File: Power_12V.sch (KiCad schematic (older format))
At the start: 5 parts

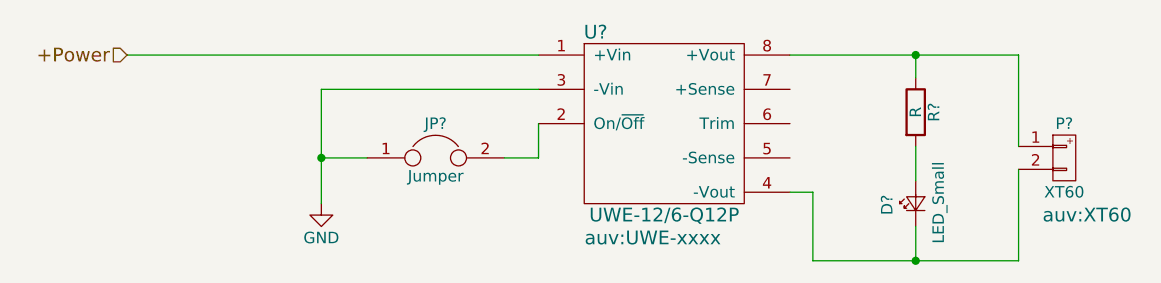
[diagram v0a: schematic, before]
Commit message: assign component value and change BC847B to BC817-40
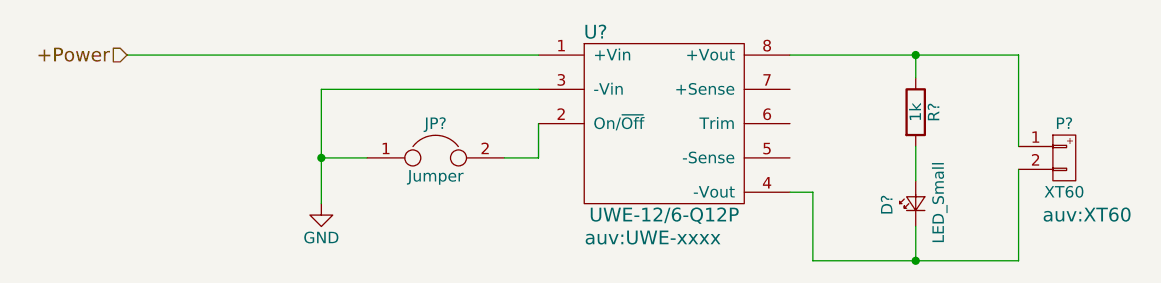
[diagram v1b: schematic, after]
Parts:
- R?: value R -> 1k
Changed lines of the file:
@@
 P 6700 3350
 F 0 "R?" V 6780 3350 50  0000 C CNN
-F 1 "R" V 6700 3350 50  0000 C CNN
+F 1 "1k" V 6700 3350 50  0000 C CNN
 F 2 "Resistors_SMD:R_0603" V 6630 3350 50  0001 C CNN
 F 3 "" H 6700 3350 50  0001 C CNN
